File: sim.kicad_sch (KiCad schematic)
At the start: 25 parts, among them J4 Antenna_connector, J5 Micro_SIM_card, Q1 Q_NPN, U2 SIM800C

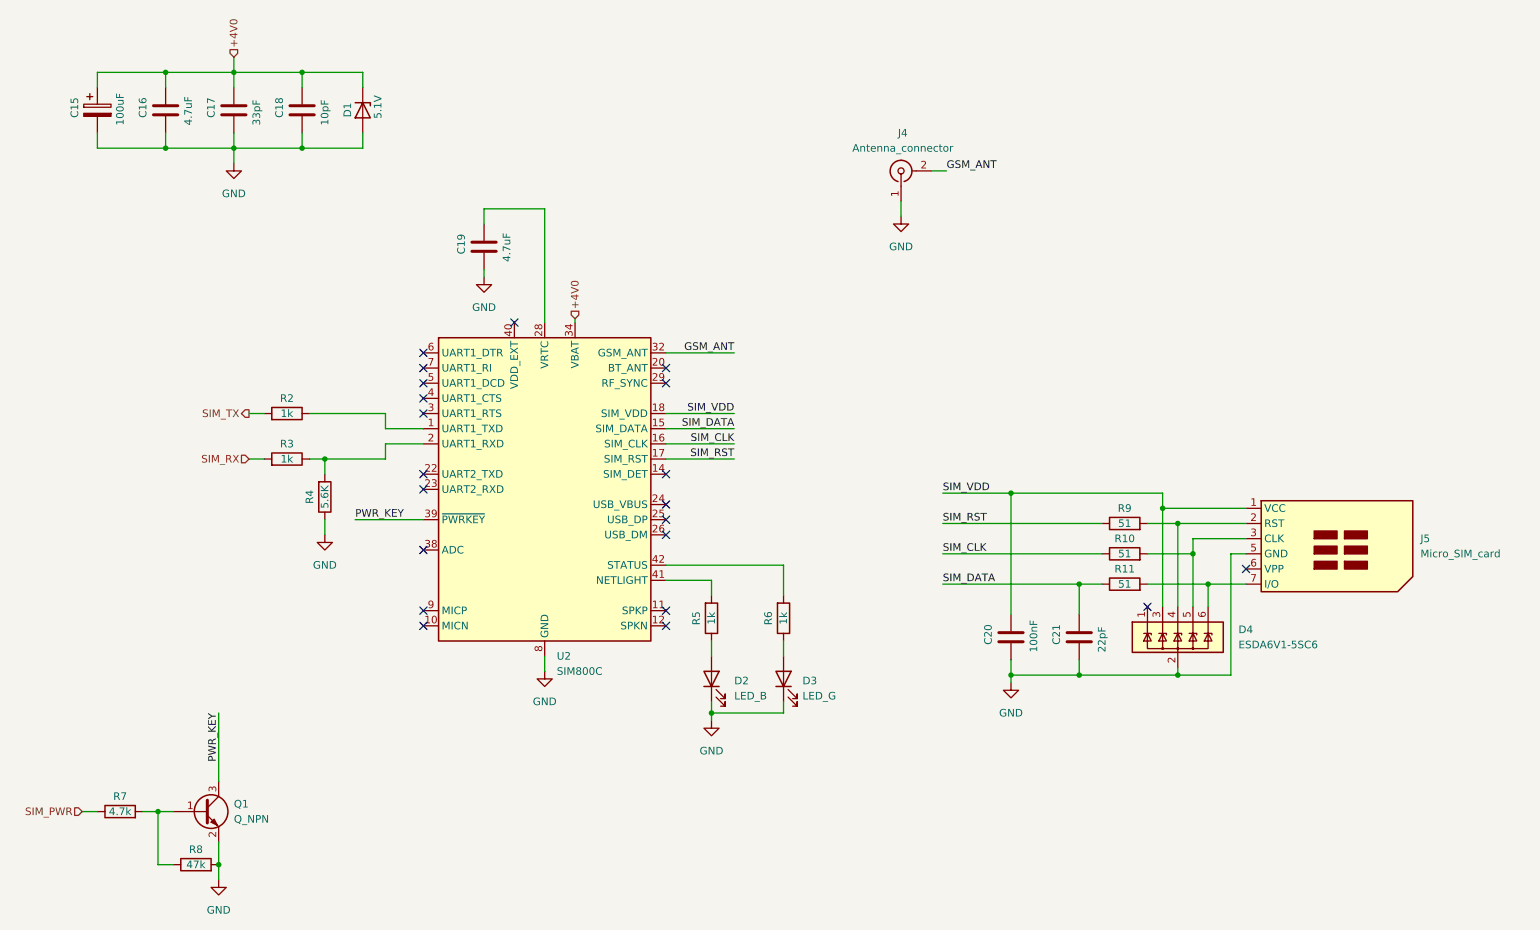
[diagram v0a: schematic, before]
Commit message: Complete the schematic, Begin to layout elements
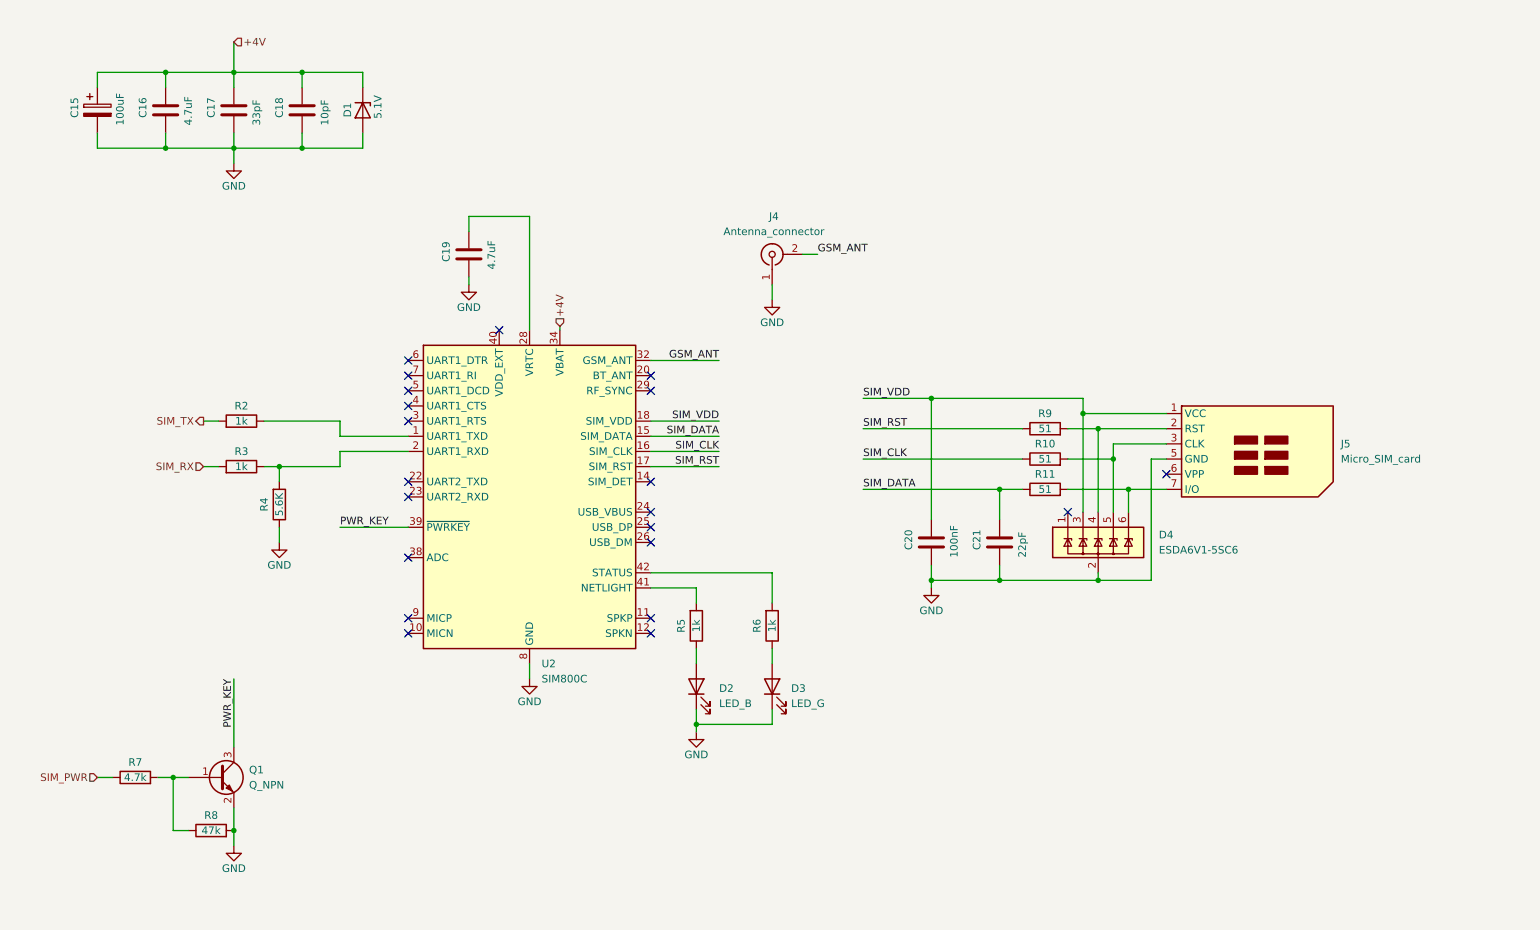
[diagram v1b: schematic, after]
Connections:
- net +4V0 renamed +4V
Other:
- moved on the sheet: C19, C20, C21, D2, D3, D4, J4, J5, Q1, R10, R11, R2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

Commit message: Partial layout
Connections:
- net GND: now also J5.SH
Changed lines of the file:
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@@
   (junction (at 184.15 87.63) (diameter 0) (color 0 0 0 0)
+  )
+  (junction (at 220.98 105.41) (diameter 0) (color 0 0 0 0)
   )
   (junction (at 74.93 99.06) (diameter 0) (color 0 0 0 0)
@@
     (stroke (width 0) (type default))
   )
+  (wire (pts (xy 220.98 105.41) (xy 223.52 105.41))
+    (stroke (width 0) (type default))
+  )
   (wire (pts (xy 64.77 99.06) (xy 62.23 99.06))
     (stroke (width 0) (type default))
@@
     (stroke (width 0) (type default))
   )
+  (wire (pts (xy 220.98 105.41) (xy 220.98 118.11))
+    (stroke (width 0) (type default))
+  )
   (wire (pts (xy 116.84 57.15) (xy 116.84 76.2))
     (stroke (width 0) (type default))
@@
     (stroke (width 0) (type default))
   )
-  (wire (pts (xy 220.98 97.79) (xy 220.98 118.11))
+  (wire (pts (xy 220.98 97.79) (xy 220.98 105.41))
     (stroke (width 0) (type default))
   )
@@
     (pin "6")
     (pin "7")
+    (pin "SH")
     (instances
       (project "Mobile_Camera"

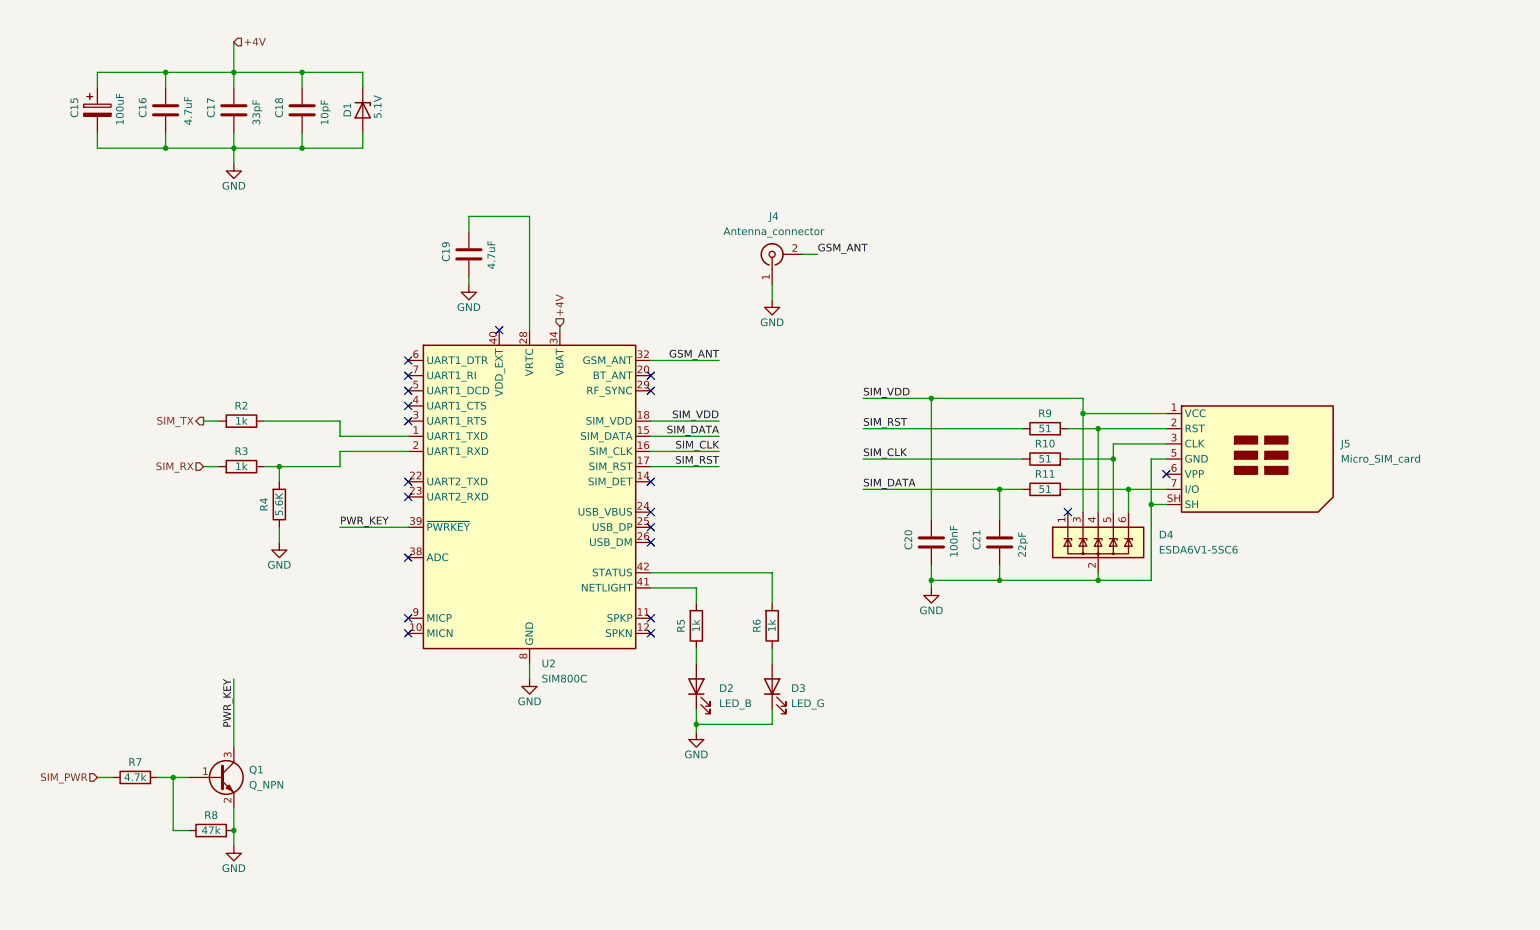
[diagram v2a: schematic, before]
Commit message: Add layout and ednge cut
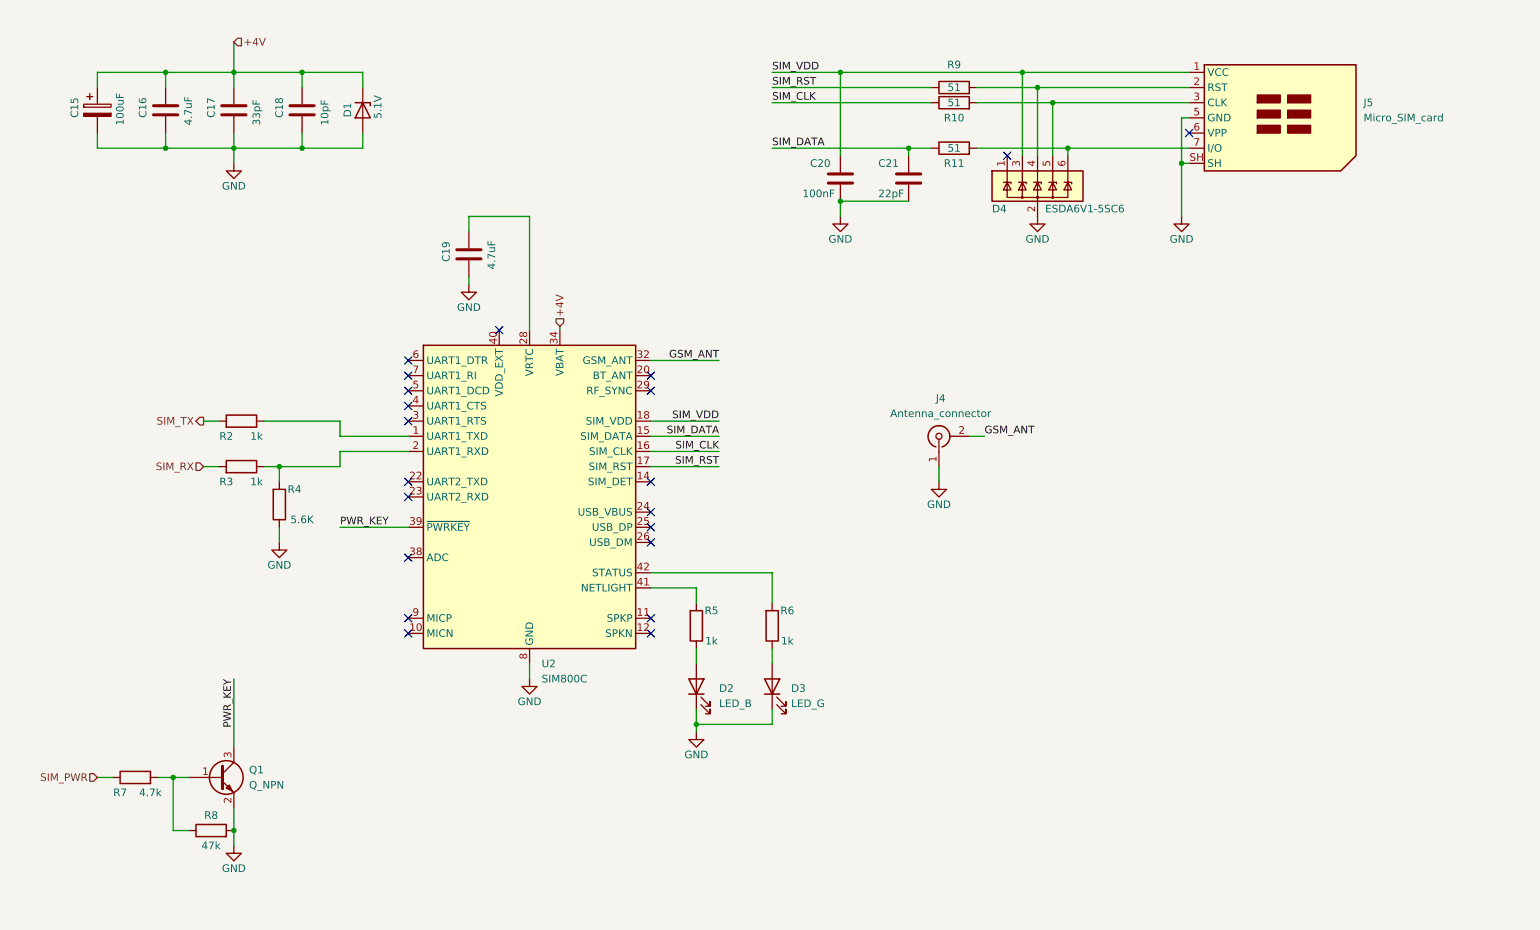
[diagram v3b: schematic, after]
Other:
- moved on the sheet: C20, C21, D4, J4, J5, R10, R11, R9

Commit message: Complete the PCB design
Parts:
- J4: footprint Connector_Coaxial:U.FL_Molex_MCRF_73412-0110_Vertical -> Connector_Coaxial:U.FL_Hirose_U.FL-R-SMT-1_Vertical
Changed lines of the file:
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@@
       (effects (font (size 1.27 1.27)))
     )
-    (property "Footprint" "Connector_Coaxial:U.FL_Molex_MCRF_73412-0110_Vertical" (at 185.42 93.98 0)
+    (property "Footprint" "Connector_Coaxial:U.FL_Hirose_U.FL-R-SMT-1_Vertical" (at 185.42 93.98 0)
       (effects (font (size 1.27 1.27)) hide)
     )
